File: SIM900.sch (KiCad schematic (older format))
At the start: 69 parts, among them J1 Conn_01x01, J2 Conn_01x07, J3 Conn_01x04, J4 Conn_01x04, J5 Conn_01x02, J6 Conn_01x12, J7 Conn_01x03, J8 Conn_Coaxial_x2_Isolated, J9 SIM_Card, Q1 Q_NPN_BCE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

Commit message: Se realizaron las modificaciones de los comentarios hechos en la planilla de revision
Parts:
- removed C20, C22: 0, symbol Device:C
- removed J1: Conn_01x01, symbol Connector_Generic:Conn_01x01
- removed J4: Conn_01x04, symbol Connector_Generic:Conn_01x04
- removed J6: Conn_01x12, symbol Connector_Generic:Conn_01x12
- removed JP1: Jumper, symbol Device:Jumper
- removed LS1: Speaker, symbol Device:Speaker
- removed MK1: Microphone, symbol Device:Microphone
- removed R14: 0, symbol Device:R
- removed R16: 10K, symbol Device:R
- removed SW2: SW_DIP_x01, symbol Switch:SW_DIP_x01
- added J1: Conn_01x05, Connector_PinSocket_1.00mm:PinSocket_1x05_P1.00mm_Vertical, symbol Connector_Generic:Conn_01x05
- added J10: Conn_01x02, Connector_PinSocket_2.00mm:PinSocket_1x02_P2.00mm_Vertical, symbol Connector_Generic:Conn_01x02
- added J11: Conn_Coaxial_Power, Connector_Coaxial:SMA_Molex_73251-2200_Horizontal, symbol Connector:Conn_Coaxial_Power
- added J12, J13: AudioJack2_Ground, Connector_Audio:Jack_3.5mm_CUI_SJ-3523-SMT_Horizontal, symbol Connector:AudioJack2_Ground
- added J4, J6: Conn_01x06, Connector_PinSocket_1.00mm:PinSocket_1x06_P1.00mm_Vertical, symbol Connector_Generic:Conn_01x06
- C1, C10, C11, C12, C13, C14, C15, C16, C17, C18, C19, C2, C3, C5, C6, C7, C8: footprint (none) -> Capacitor_Tantalum_SMD:CP_EIA-2012-12_Kemet-R_Pad1.30x1.05mm_HandSolder
- C20: renamed from C21; footprint (none) -> Capacitor_Tantalum_SMD:CP_EIA-2012-12_Kemet-R_Pad1.30x1.05mm_HandSolder
- C4, C9: footprint (none) -> Capacitor_SMD:CP_Elec_4x3
- D1, D11, D2, D4, D5: footprint (none) -> Diode_SMD:D_SMC
- D3, D6: footprint (none) -> LED_SMD:LED_0603_1608Metric_Pad1.05x0.95mm_HandSolder
- J2: footprint (none) -> Connector_PinSocket_1.00mm:PinSocket_1x07_P1.00mm_Vertical
- J3: footprint (none) -> Connector_PinSocket_1.00mm:PinSocket_1x04_P1.00mm_Vertical
- J5: footprint (none) -> Connector_JST:JST_EH_S2B-EH_1x02_P2.50mm_Horizontal
- J7: footprint (none) -> Connector_PinSocket_1.00mm:PinSocket_1x03_P1.00mm_Vertical
- J8: footprint (none) -> Connector_Coaxial:U.FL_Hirose_U.FL-R-SMT-1_Vertical
- J9: footprint (none) -> Connector_Card:microSD_HC_Hirose_DM3D-SF
- L1: footprint (none) -> Inductor_SMD:L_0603_1608Metric_Pad1.05x0.95mm_HandSolder
- Q1, Q2, Q3: footprint (none) -> Package_TO_SOT_SMD:SOT-23W
- R1, R10, R11, R12, R13, R15, R2, R3, R4, R5, R6, R7, R8, R9: footprint (none) -> Resistor_SMD:R_0603_1608Metric_Pad1.05x0.95mm_HandSolder
- SW1: footprint (none) -> Button_Switch_THT:SW_Tactile_SPST_Angled_PTS645Vx31-2LFS
- U1: footprint Package_TO_SOT_THT:TO-220-5_P3.4x3.7mm_StaggerEven_Lead3.8mm_Vertical -> Package_TO_SOT_SMD:TO-263-5_TabPin3
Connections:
- net labels added: RST_EXT
- net labels removed: DC_INPUT, PWR_CTRL
- wire segments 231 -> 254
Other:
- note added: "NOTA:\n1.-El capacitor de 100uF debe ser colocado lo mas cerca del modulos SIM900.\n2.-El conector de Test RF debe estar lo mas cerca posible del modulo SIM900.\n3.-Los componentes deben estar tan cerca del microfono y spiker de ser posible.\n4.-Ambos tipos de lineas deben colocarse siguiedo las reglas de diferencial de lineas.\n"
- note removed: "POWER CIRCUIT"
- moved on the sheet: C18, C4, C8, J8A, R15

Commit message: Se incluyo el poncho de la EDU CIAA y se ordenaron los componentes dentro de ella
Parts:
- removed J10: Conn_01x02, Connector_PinSocket_2.00mm:PinSocket_1x02_P2.00mm_Vertical, symbol Connector_Generic:Conn_01x02
- removed J2: Conn_01x07, Connector_PinSocket_1.00mm:PinSocket_1x07_P1.00mm_Vertical, symbol Connector_Generic:Conn_01x07
- added J2: Conn_01x04, Connector_PinSocket_1.00mm:PinSocket_1x04_P1.00mm_Vertical, symbol Connector_Generic:Conn_01x04
- added XA1: Conn_Poncho2P_2x_20x2, Poncho_Esqueleto:Conn_Poncho_Completo, symbol Poncho_Esqueleto:Conn_Poncho2P_2x_20x2
- J11: footprint Connector_Coaxial:SMA_Molex_73251-2200_Horizontal -> Connector_Coaxial:U.FL_Hirose_U.FL-R-SMT-1_Vertical
- J8: footprint Connector_Coaxial:U.FL_Hirose_U.FL-R-SMT-1_Vertical -> Connector_Coaxial:SMA_Amphenol_132203-12_Horizontal
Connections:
- net labels added: +3.3V, GNDA, RXD, TXD, VCD_5V
- wire segments 254 -> 321
- no-connect marks 2 -> 47
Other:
- note added: "EDUCIAA CIRCUIT EXTERN"
- moved on the sheet: C17, C18, C19, C20, D10, D11, D3, D6, D7, D8, D9, J11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

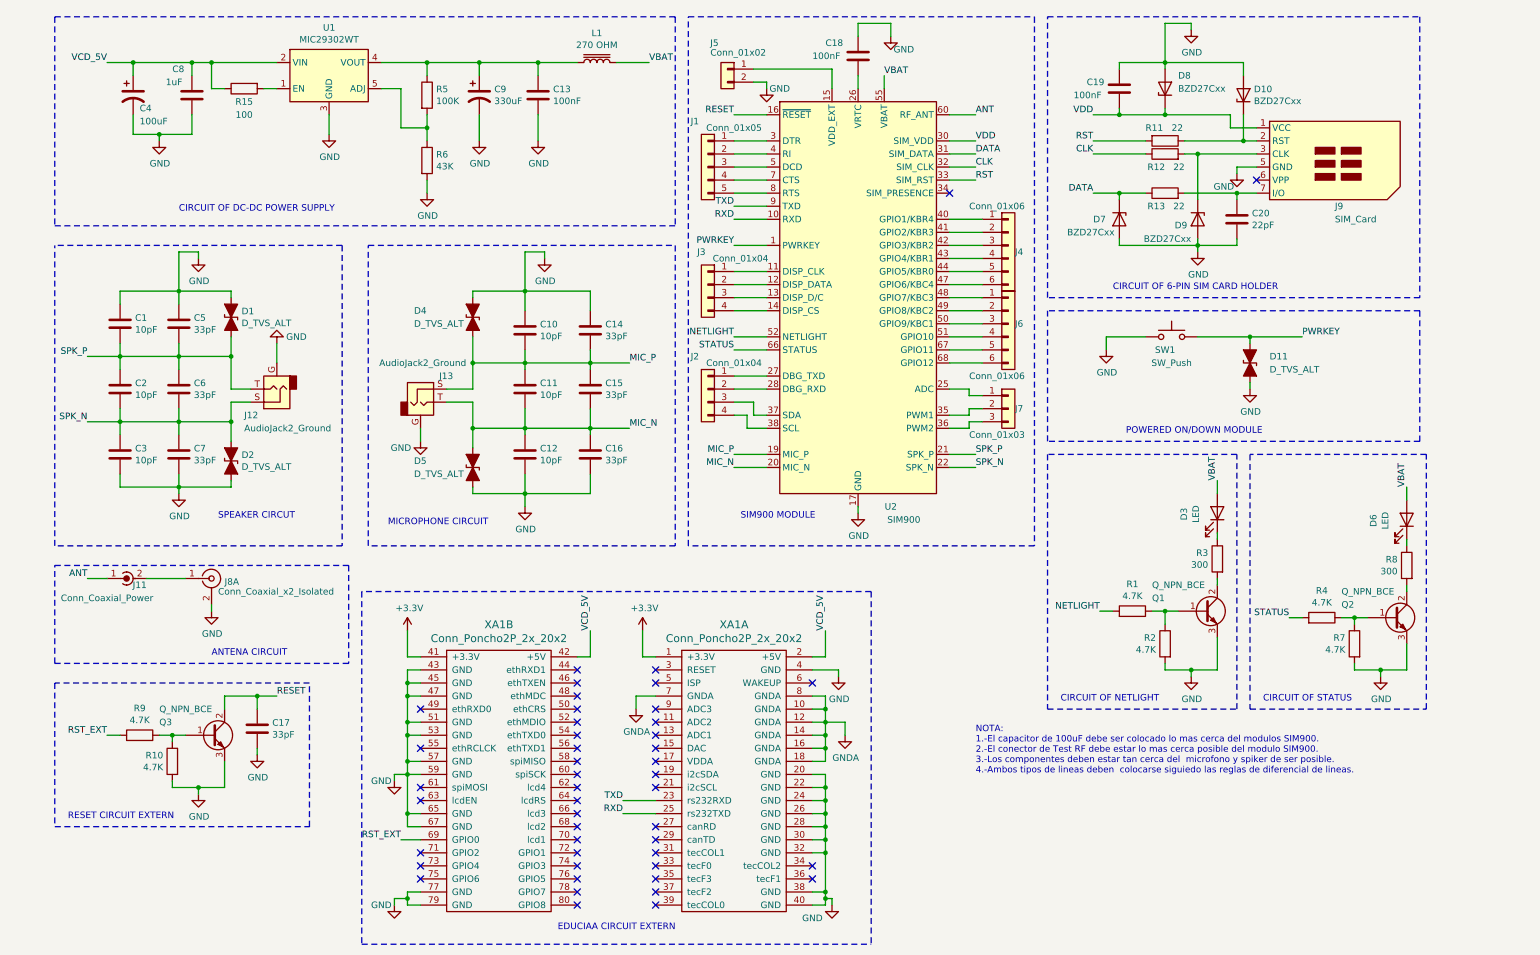
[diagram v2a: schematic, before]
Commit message: Se ordeno mejor los componentes y se redujo la planilla de la EDU CIAA
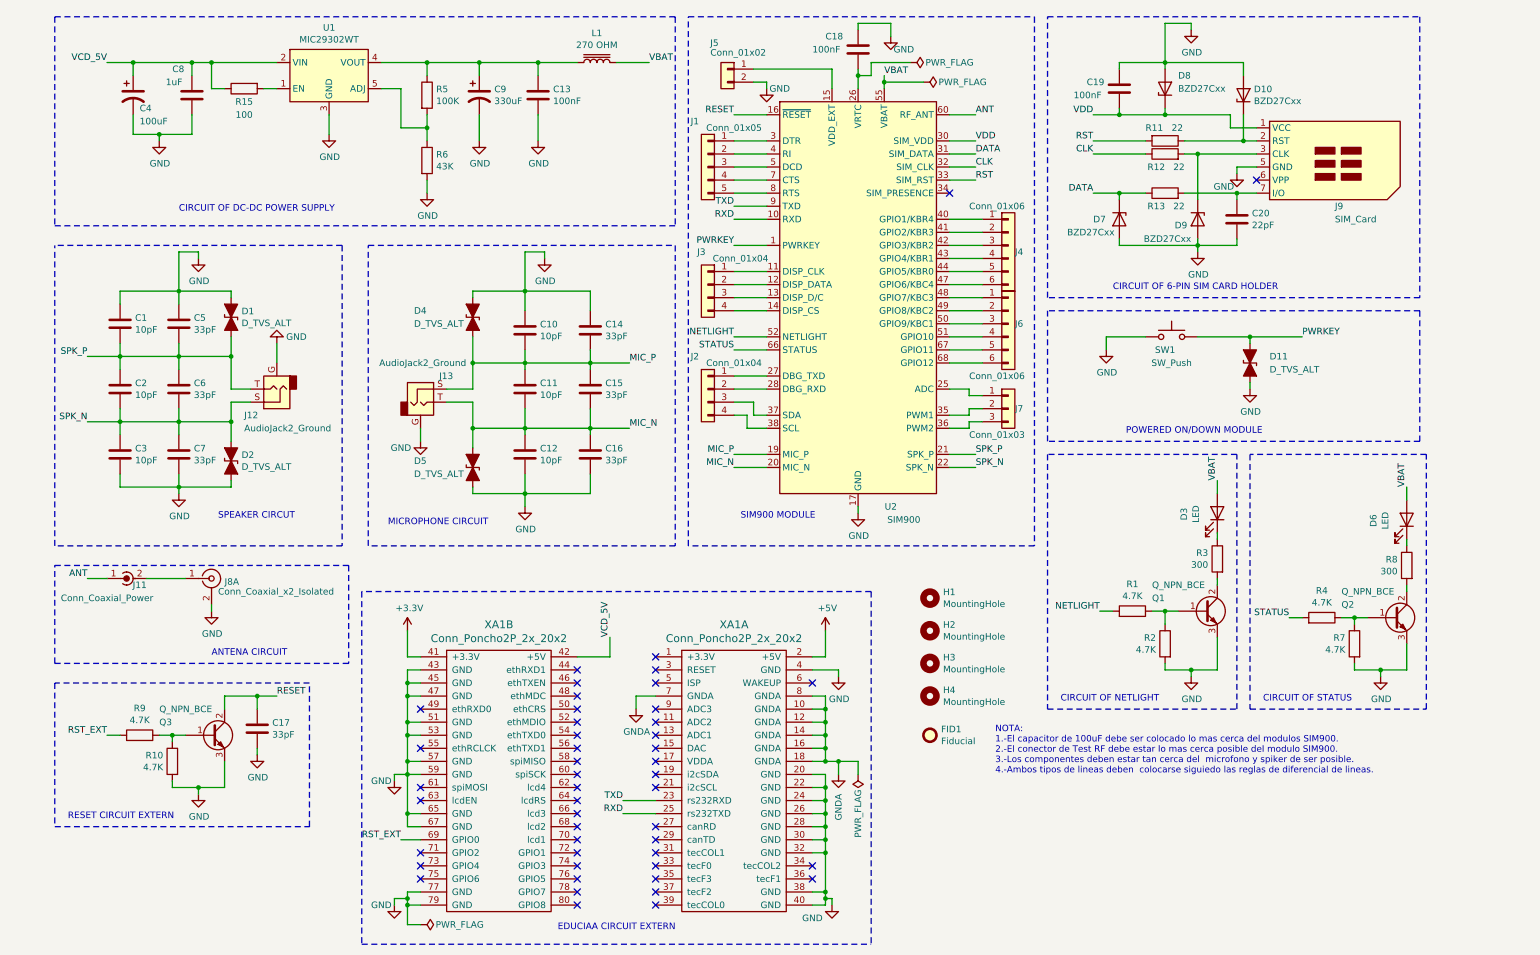
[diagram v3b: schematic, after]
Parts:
- added FID1: Fiducial, Fiducial:Fiducial_0.75mm_Mask2.25mm, symbol Mechanical:Fiducial
- added H1, H2, H3, H4: MountingHole, MountingHole:MountingHole_2.5mm_Pad, symbol Mechanical:MountingHole
- D1, D11, D2, D4, D5: footprint Diode_SMD:D_SMC -> Diode_SMD:D_SMA_Handsoldering
- D3, D6: footprint LED_SMD:LED_0603_1608Metric_Pad1.05x0.95mm_HandSolder -> LED_SMD:LED_0805_2012Metric
- J1: footprint Connector_PinSocket_1.00mm:PinSocket_1x05_P1.00mm_Vertical -> Connector_PinHeader_2.00mm:PinHeader_1x05_P2.00mm_Vertical
- J2, J3: footprint Connector_PinSocket_1.00mm:PinSocket_1x04_P1.00mm_Vertical -> Connector_PinHeader_2.00mm:PinHeader_1x04_P2.00mm_Vertical
- J4, J6: footprint Connector_PinSocket_1.00mm:PinSocket_1x06_P1.00mm_Vertical -> Connector_PinHeader_2.00mm:PinHeader_1x06_P2.00mm_Vertical
- J7: footprint Connector_PinSocket_1.00mm:PinSocket_1x03_P1.00mm_Vertical -> Connector_PinHeader_2.00mm:PinHeader_1x03_P2.00mm_Vertical
- R1, R10, R11, R12, R13, R15, R2, R3, R4, R5, R6, R7, R8, R9: footprint Resistor_SMD:R_0603_1608Metric_Pad1.05x0.95mm_HandSolder -> Resistor_SMD:R_0805_2012Metric_Pad1.15x1.40mm_HandSolder
- XA1: footprint Poncho_Esqueleto:Conn_Poncho_Completo -> Poncho_Esqueleto:Conn_Poncho_Chico
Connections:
- net +3V3: no longer XA1.1 (+3.3V)
- net VCD_5V: no longer XA1.2 (+5V)
- new net +5V: XA1.2 (+5V)
- no-connect marks 47 -> 48
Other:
- moved on the sheet: C18

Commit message: Se completo el PCB y se corrigieron la mayoria de las observaciones del profeor
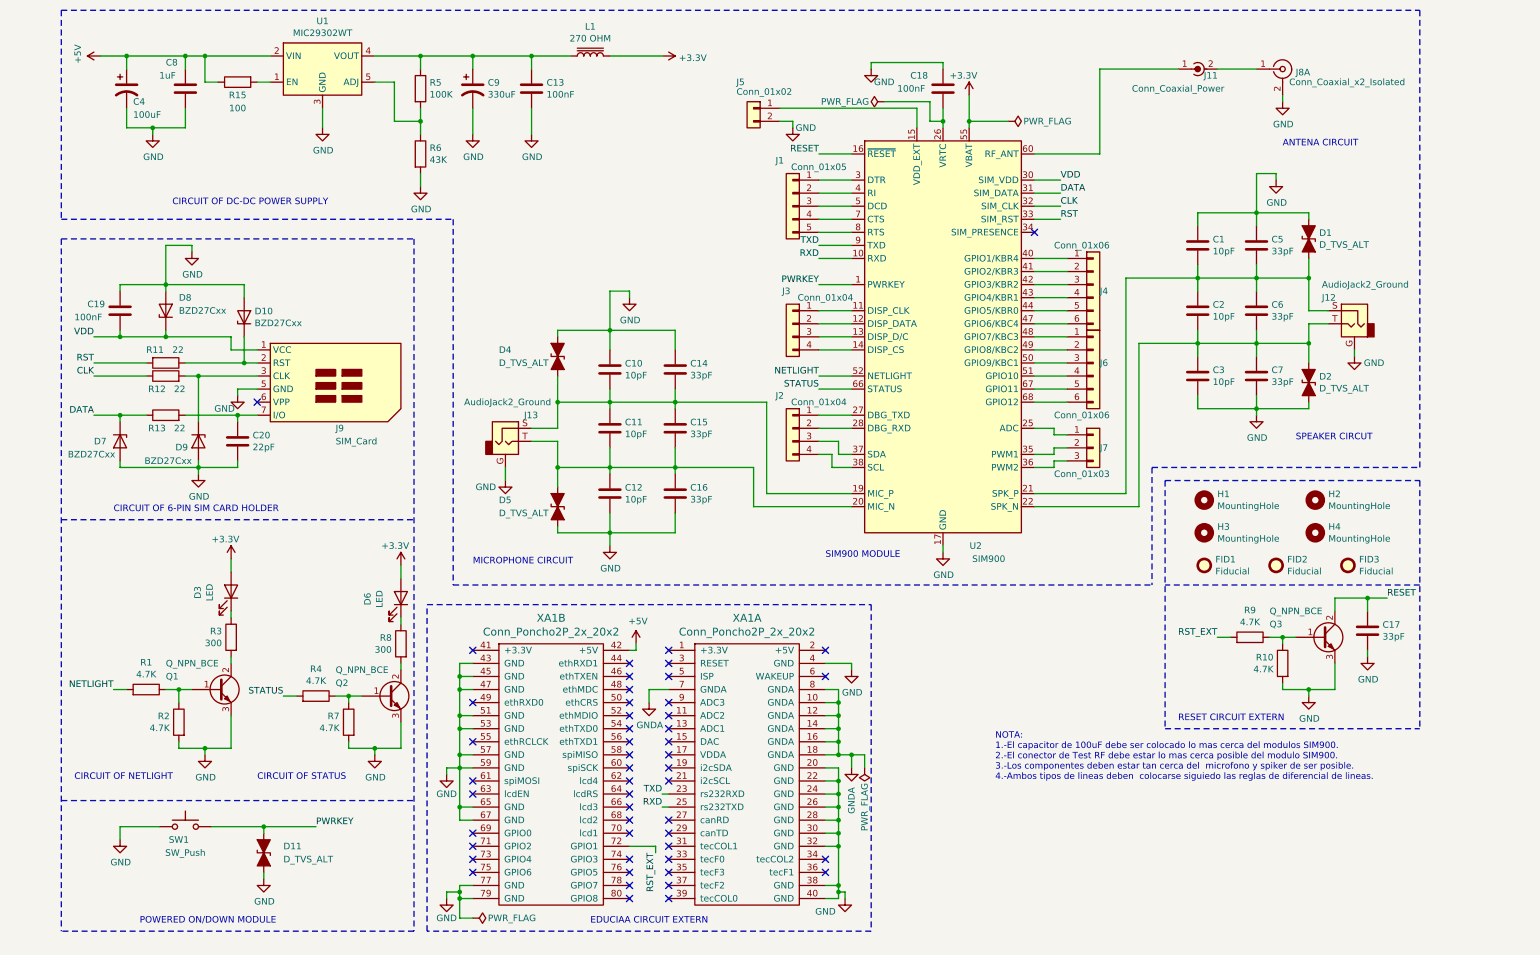
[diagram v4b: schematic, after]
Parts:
- added FID2, FID3: Fiducial, Fiducial:Fiducial_0.75mm_Mask2.25mm, symbol Mechanical:Fiducial
- C1, C10, C11, C12, C13, C14, C15, C16, C17, C18, C19, C2, C20, C3, C5, C6, C7, C8: footprint Capacitor_Tantalum_SMD:CP_EIA-2012-12_Kemet-R_Pad1.30x1.05mm_HandSolder -> Capacitor_SMD:C_0805_2012Metric
- C4, C9: footprint Capacitor_SMD:CP_Elec_4x3 -> Capacitor_SMD:C_0805_2012Metric
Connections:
- net VBAT is gone; now on net +3V3: D3.2 (A), D6.2 (A), L1.2, U2.55 (VBAT), U2.56 (VBAT), U2.57 (VBAT)
- net VCD_5V is gone; now on net +5V: C4.1, C8.1, R15.1, U1.2 (VIN), XA1.42 (+5V)
- net +3V3: no longer XA1.41 (+3.3V)
- net +5V: no longer XA1.2 (+5V)
- net RST_EXT: now also XA1.72 (GPIO1); no longer XA1.69 (GPIO0)
- net ANT: no longer names the net of J11.1 (In), U2.60 (RF_ANT)
- net MIC_N: no longer names the net of C11.1, C12.1, C15.1, C16.1, D5.1 (A1), J13.T, U2.20 (MIC_N)
- net MIC_P: no longer names the net of C10.1, C11.2, C14.1, C15.2, D4.2 (A2), J13.S, U2.19 (MIC_P)
- net SPK_N: no longer names the net of C2.1, C3.1, C6.1, C7.1, D2.1 (A1), U2.22 (SPK_N)
- net SPK_N: now also J12.T; no longer J12.S
- net SPK_P: no longer names the net of C1.1, C2.2, C5.1, C6.2, D1.2 (A2), U2.21 (SPK_P)
- net SPK_P: now also J12.S; no longer J12.T
- no-connect marks 48 -> 50
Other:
- moved on the sheet: C1, C10, C11, C12, C13, C14, C15, C16, C17, C18, C19, C2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

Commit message: Se mejoro el conexionado en el PCB
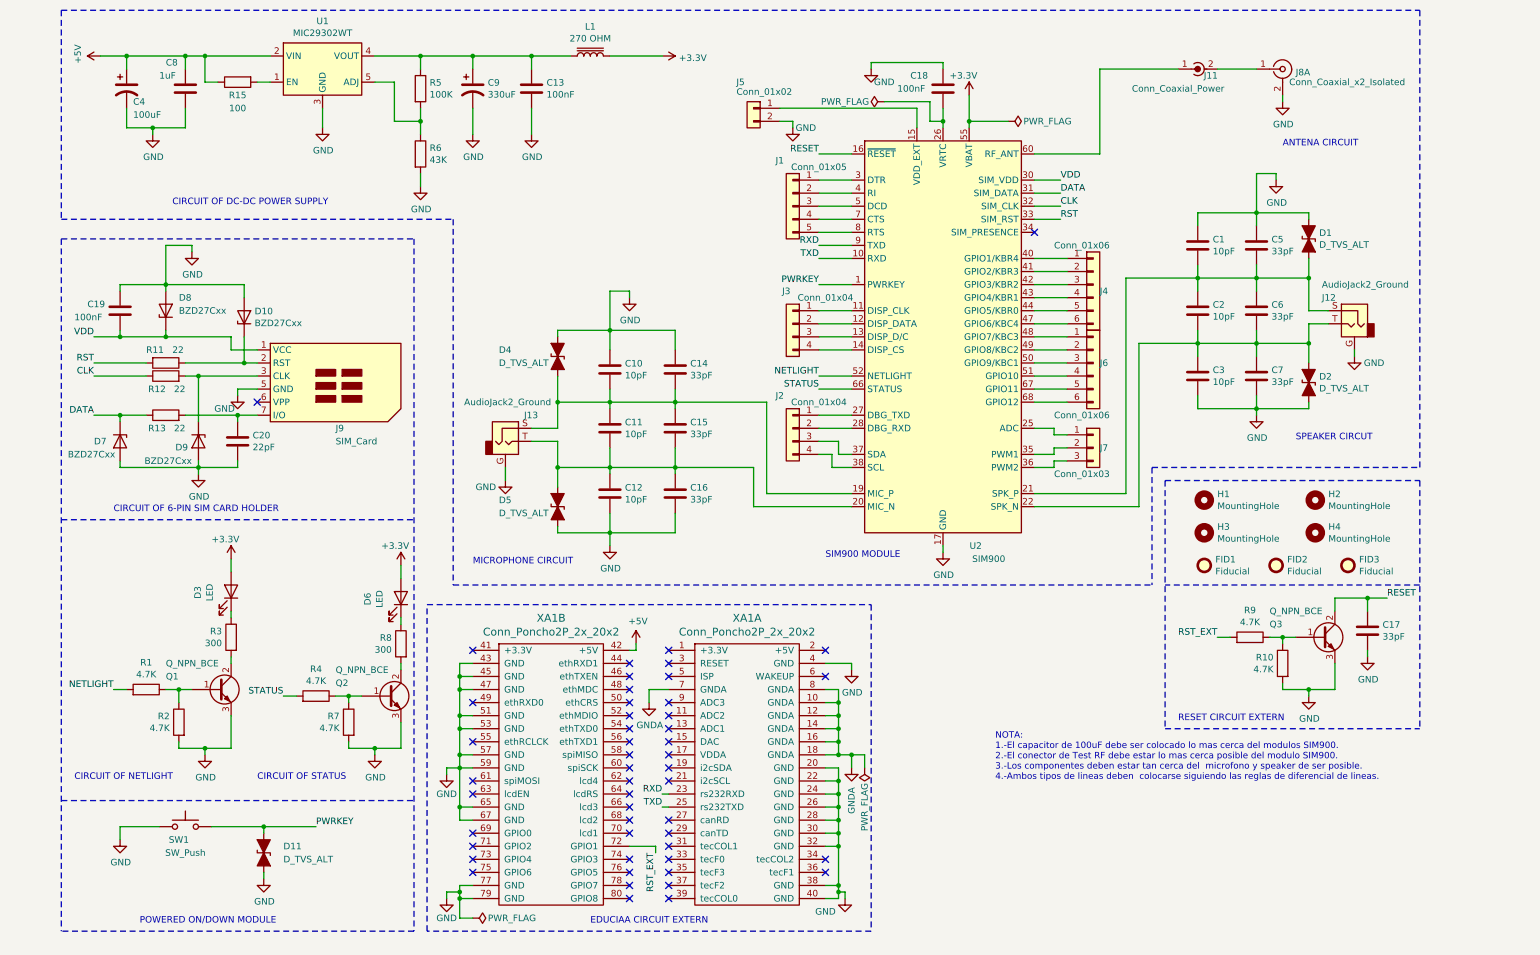
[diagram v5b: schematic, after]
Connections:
- net RXD: now also U2.9 (TXD), XA1.23 (rs232RXD); no longer U2.10 (RXD), XA1.25 (rs232TXD)
- net TXD: now also U2.10 (RXD), XA1.25 (rs232TXD); no longer U2.9 (TXD), XA1.23 (rs232RXD)
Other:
- note added: "NOTA:\n1.-El capacitor de 100uF debe ser colocado lo mas cerca del modulos SIM900.\n2.-El conector de Test RF debe estar lo mas cerca posible del modulo SIM900.\n3.-Los componentes deben estar tan cerca del microfono y speaker de ser posible.\n4.-Ambos tipos de lineas deben colocarse siguiendo las reglas de diferencial de lineas.\n"
- note removed: "NOTA:\n1.-El capacitor de 100uF debe ser colocado lo mas cerca del modulos SIM900.\n2.-El conector de Test RF debe estar lo mas cerca posible del modulo SIM900.\n3.-Los componentes deben estar tan cerca del microfono y spiker de ser posible.\n4.-Ambos tipos de lineas deben colocarse siguiedo las reglas de diferencial de lineas.\n"
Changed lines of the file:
@@
 	4850 2750 4850 3050
 Text Notes 7800 6500 0    49   ~ 0
-NOTA:\n1.-El capacitor de 100uF debe ser colocado lo mas cerca del modulos SIM900.\n2.-El conector de Test RF debe estar lo mas cerca posible del modulo SIM900.\n3.-Los componentes deben estar tan cerca del  microfono y spiker de ser posible.\n4.-Ambos tipos de lineas deben  colocarse siguiedo las reglas de diferencial de lineas.\n
+NOTA:\n1.-El capacitor de 100uF debe ser colocado lo mas cerca del modulos SIM900.\n2.-El conector de Test RF debe estar lo mas cerca posible del modulo SIM900.\n3.-Los componentes deben estar tan cerca del  microfono y speaker de ser posible.\n4.-Ambos tipos de lineas deben  colocarse siguiendo las reglas de diferencial de lineas.\n
 $Comp
 L Poncho_Esqueleto:Conn_Poncho2P_2x_20x2 XA1
@@
 	-1   0    0    -1
 $EndComp
+Text Label 6450 2500 2    50   ~ 0
+TXD
 Text Label 6450 2400 2    50   ~ 0
+RXD
+Wire Wire Line
+	6450 3700 6700 3700
+Wire Wire Line
+	6450 3800 6700 3800
+Wire Wire Line
+	6450 3900 6600 3900
+Wire Wire Line
+	6600 3900 6600 4000
+Wire Wire Line
+	6600 4000 6700 4000
+Wire Wire Line
+	6450 4000 6550 4000
+Wire Wire Line
+	6550 4000 6550 4100
+Wire Wire Line
+	6550 4100 6700 4100
+Text Label 5250 6700 2    50   ~ 0
 TXD
-Text Label 6450 2500 2    50   ~ 0
-RXD
-Wire Wire Line
-	6450 3700 6700 3700
-Wire Wire Line
-	6450 3800 6700 3800
-Wire Wire Line
-	6450 3900 6600 3900
-Wire Wire Line
-	6600 3900 6600 4000
-Wire Wire Line
-	6600 4000 6700 4000
-Wire Wire Line
-	6450 4000 6550 4000
-Wire Wire Line
-	6550 4000 6550 4100
-Wire Wire Line
-	6550 4100 6700 4100
 Text Label 5250 6600 2    50   ~ 0
-TXD
-Text Label 5250 6700 2    50   ~ 0
 RXD
 NoConn ~ 5300 6400
